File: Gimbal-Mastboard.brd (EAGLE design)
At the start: 51.5 x 57.3 mm, 20 parts, among them J1 SL04, J2 APP_2POS_CONFIG12V_HORIZ, U1 OKI-78SR-5/1.5-W36HC, U2 LP2985-33DBVR, Y2 CSTCE16M0V53-R0 16MHZ

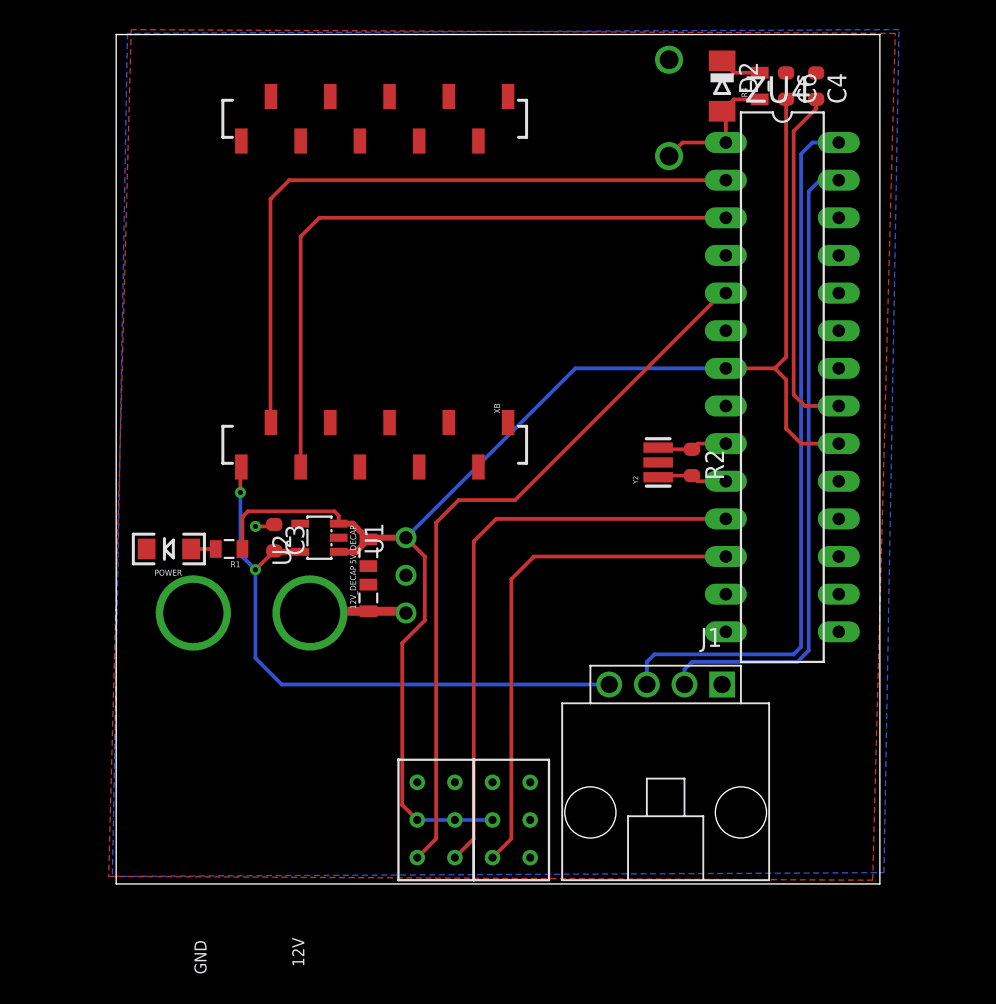
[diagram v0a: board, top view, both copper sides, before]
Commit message: Updated schematic and board for final board review
Changed oscilator for ATMEGA
changed power to ATMEGA to 3.3V
Cleaned up position and traces
Added mounting holes
Added signature and board data
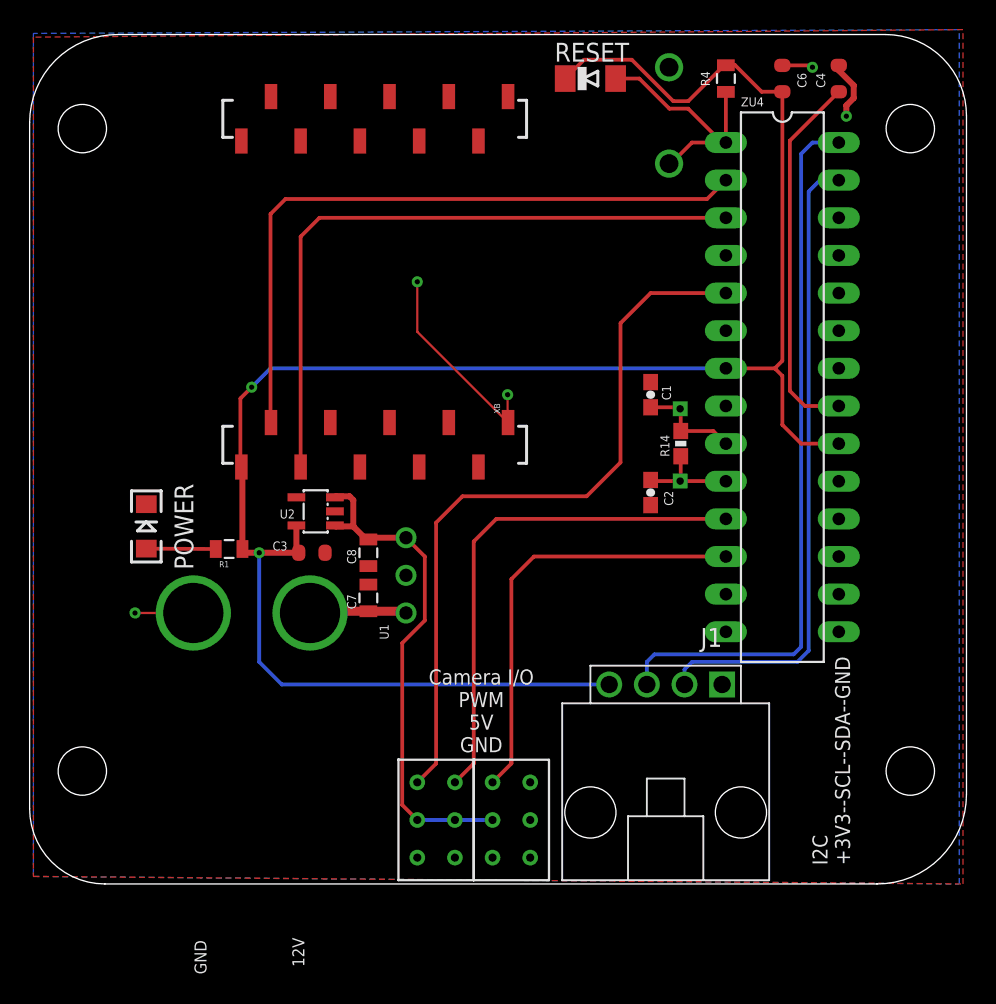
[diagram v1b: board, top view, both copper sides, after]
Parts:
- removed D2: CD1206-S01575, diode:MINIMELF
- removed R2: 1M, SmartPrj:R0603-ROUND
- removed Y2: CSTCE16M0V53-R0 16MHZ, SmartPrj:RESONATOR
- added C1, C2: 22p, SparkFun-Passives:0603-CAP
- added H1, H2, H3, H4: MOUNTING_HOLE#4, MRDT-Hardware:#4_SCREW
- added LOGO1: MRDT_LOGO, MRDT-Hardware:MRDT_LOGO
- added R14: 1M, SparkFun-Resistors:0603-RES
- added RESET: CD1206-S01575, diode:MINIMELF
- added U$3: ANDREW_VAN_HORN_SIGNATURE, MRDT-Signatures:ANDREW_VAN_HORN_SIGNATURE
- added X1: X_HC49SCRYSTAL, MRDT-2014-All:HC-49
- moved C3 2.74 mm to (13.2, 22.4), turned to 180 degrees
- moved R4 2.34 mm to (41.1, 54.4)
- moved POWER 2.16 mm to (2.03, 24.1), turned to 90 degrees
- moved U2 1.80 mm to (13.5, 25.1)
- moved C4 1.61 mm to (48.8, 54.4)
- moved C6 0.57 mm to (45.0, 54.4)
- moved S1 0.51 mm to (35.6, 54.9)
- renumbered 12V_DECAP to C7, 5V_DECAP to C8
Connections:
- net N$5 renamed 12V
- removed net XTAL1: R2.1, Y2.3, ZU4.9
- removed net XTAL2: R2.2, Y2.1, ZU4.10
- new net N$1: C2.2, R14.1, X1.P$2, ZU4.10
- new net N$10: C1.2, R14.2, X1.P$1, ZU4.9
- net +3V3: now also C6.2, R1.1, R4.2, RESET.C, ZU4.20, ZU4.7
- net +5V: no longer C6.2, D2.C, R1.1, R4.2, ZU4.20, ZU4.7
- net GND: now also C1.1, C2.1, U$1.P$3, U$2.P$3, U$2.P$6; no longer U$1.P$1, U$2.P$1, U$2.P$4, Y2.2
- net PWM_1: now also U$2.P$1; no longer U$2.P$3
- net PWM_2: now also U$2.P$4; no longer U$2.P$6
- net PWM_3: now also U$1.P$1; no longer U$1.P$3
- net RESET: now also RESET.A; no longer D2.A
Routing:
- net +3V3: track 41.5 -> 130.2 mm
- net +5V: track 101.9 -> 34.1 mm
- net GND: track 1.32 -> 24.0 mm, vias 1 -> 5
- net RESET: track 9.30 -> 17.1 mm
- net N$10: track 0.00 -> 6.95 mm
- net N$1: track 0.00 -> 6.81 mm
- net PWM_3: track 34.4 -> 29.6 mm
- net PWM_2: track 39.5 -> 34.7 mm
- net XTAL2: track 4.78 -> 0.00 mm
- net XTAL1: track 4.78 -> 0.00 mm
- net N$17: track 1.66 -> 4.69 mm
- net AREF: track 23.9 -> 25.3 mm
- net XB_RX: track 46.4 -> 45.8 mm
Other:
- board size 51.5 x 57.3 mm -> 63.2 x 57.3 mm
- board text added: "Camera I/O PWM 5V GND"
- board text added: "Gimbal Mastboard Rev 1 Mars Rover 2018 Missouri S&T Andrew Van Horn"
- board text added: "I2C +3V3--SCL--SDA--GND"

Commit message: Final board review and Rev 1 Gerbs
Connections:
- net RESET renamed N$2
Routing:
- net GND: track 24.0 -> 6.14 mm
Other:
- board text added: "<--"
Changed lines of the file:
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@@
 Missouri S&amp;T
 Andrew Van Horn</text>
+<text x="31.496" y="8.636" size="1.778" layer="25" rot="R90">&lt;--
+</text>
 </plain>
 <attributes>
@@
 <wire x1="49.276" y1="52.53973125" x2="49.276" y2="51.816" width="0.4064" layer="1"/>
 <via x="49.276" y="51.816" extent="1-16" drill="0.35"/>
-<wire x1="5.207" y1="18.288" x2="1.27" y2="18.288" width="0.1524" layer="1"/>
 <via x="1.27" y="18.288" extent="1-16" drill="0.35"/>
-<wire x1="26.416" y1="31.172" x2="26.448" y2="31.14" width="0.1524" layer="1"/>
-<wire x1="26.416" y1="31.172" x2="26.416" y2="33.02" width="0.1524" layer="1"/>
 <via x="26.416" y="33.02" extent="1-16" drill="0.35"/>
-<wire x1="26.448" y1="31.14" x2="20.32" y2="37.268" width="0.1524" layer="1"/>
-<wire x1="20.32" y1="37.268" x2="20.32" y2="40.64" width="0.1524" layer="1"/>
 <via x="20.32" y="40.64" extent="1-16" drill="0.35"/>
 </signal>
@@
 <wire x1="45.466" y1="50.165" x2="45.466" y2="33.274" width="0.254" layer="1"/>
 </signal>
-<signal name="RESET">
-<contactref element="ZU4" pad="1"/>
-<contactref element="RESET" pad="A"/>
-<contactref element="S1" pad="P$2"/>
-<contactref element="R4" pad="1"/>
-<wire x1="41.148" y1="50.038" x2="41.148" y2="53.456" width="0.254" layer="1"/>
-<wire x1="33.704" y1="54.356" x2="35.306" y2="54.356" width="0.254" layer="1"/>
-<wire x1="35.306" y1="54.356" x2="37.338" y2="52.324" width="0.254" layer="1"/>
-<wire x1="37.3126" y1="48.6156" x2="37.4396" y2="48.6156" width="0.254" layer="1"/>
-<wire x1="37.4396" y1="48.6156" x2="38.862" y2="50.038" width="0.254" layer="1"/>
-<wire x1="38.862" y1="50.038" x2="41.148" y2="50.038" width="0.254" layer="1"/>
-<wire x1="37.338" y1="52.324" x2="38.608" y2="52.324" width="0.254" layer="1"/>
-<wire x1="38.608" y1="52.324" x2="40.894" y2="50.038" width="0.254" layer="1"/>
-<wire x1="40.894" y1="50.038" x2="41.148" y2="50.038" width="0.254" layer="1"/>
-</signal>
 <signal name="PWM_3">
 <contactref element="ZU4" pad="12"/>
@@
 <wire x1="40.298" y1="30.568" x2="41.148" y2="29.718" width="0.254" layer="1"/>
 </signal>
+<signal name="N$2">
+<contactref element="ZU4" pad="1"/>
+<contactref element="RESET" pad="A"/>
+<wire x1="33.704" y1="54.356" x2="35.306" y2="54.356" width="0.254" layer="1"/>
+<wire x1="35.306" y1="54.356" x2="37.338" y2="52.324" width="0.254" layer="1"/>
+<wire x1="37.338" y1="52.324" x2="38.608" y2="52.324" width="0.254" layer="1"/>
+<wire x1="38.608" y1="52.324" x2="40.894" y2="50.038" width="0.254" layer="1"/>
+<wire x1="40.894" y1="50.038" x2="41.148" y2="50.038" width="0.254" layer="1"/>
+<contactref element="S1" pad="P$2"/>
+<contactref element="R4" pad="1"/>
+<wire x1="41.148" y1="53.456" x2="41.148" y2="50.038" width="0.254" layer="1"/>
+<wire x1="41.148" y1="50.038" x2="40.386" y2="50.038" width="0.254" layer="1"/>
+<wire x1="40.386" y1="50.038" x2="39.116" y2="48.768" width="0.254" layer="1"/>
+<wire x1="39.116" y1="48.768" x2="37.465" y2="48.768" width="0.254" layer="1"/>
+<wire x1="37.465" y1="48.768" x2="37.3126" y2="48.6156" width="0.254" layer="1"/>
+</signal>
 </signals>
